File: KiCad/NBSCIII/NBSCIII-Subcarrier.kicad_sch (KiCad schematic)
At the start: 7 parts, among them U4 4011, U5 4029, U6 4029, U7 4027, U8 4027

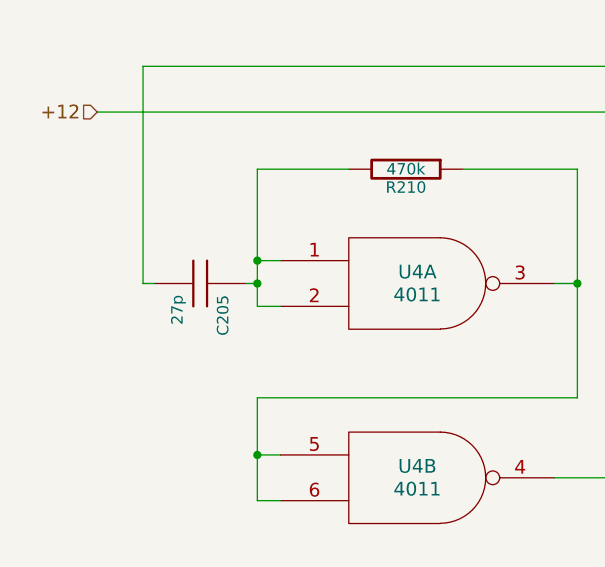
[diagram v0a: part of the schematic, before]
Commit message: unrescue to Device:C
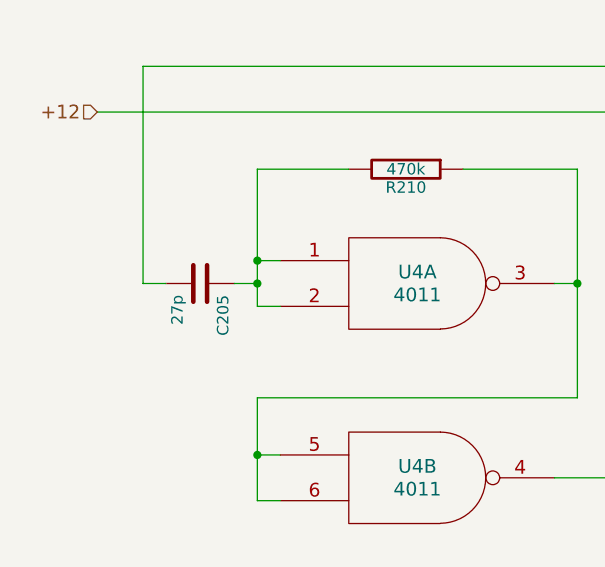
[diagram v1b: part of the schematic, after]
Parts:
- C205: symbol NBSCIII-rescue:C -> Device:C
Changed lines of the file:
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@@
-    (stroke (width 0) (type default) (color 0 0 0 0))
-  )
-  (wire (pts (xy 40.64 97.79) (xy 41.91 97.79))
     (stroke (width 0) (type default) (color 0 0 0 0))
   )
@@
     (stroke (width 0) (type default) (color 0 0 0 0))
   )
-  (wire (pts (xy 30.48 97.79) (xy 29.21 97.79))
+  (wire (pts (xy 29.21 97.79) (xy 31.75 97.79))
     (stroke (width 0) (type default) (color 0 0 0 0))
   )
@@
   )
   (wire (pts (xy 87.63 176.53) (xy 87.63 191.77))
+    (stroke (width 0) (type default) (color 0 0 0 0))
+  )
+  (wire (pts (xy 39.37 97.79) (xy 41.91 97.79))
     (stroke (width 0) (type default) (color 0 0 0 0))
   )
@@
     (pin "2")
   )
-  (symbol (lib_id "NBSCIII-rescue:C") (at 35.56 97.79 270) (unit 1)
+  (symbol (lib_id "Device:C") (at 35.56 97.79 270) (unit 1)
     (in_bom yes) (on_board yes)
     (property "Reference" "C205" (id 0) (at 38.1 99.06 0)

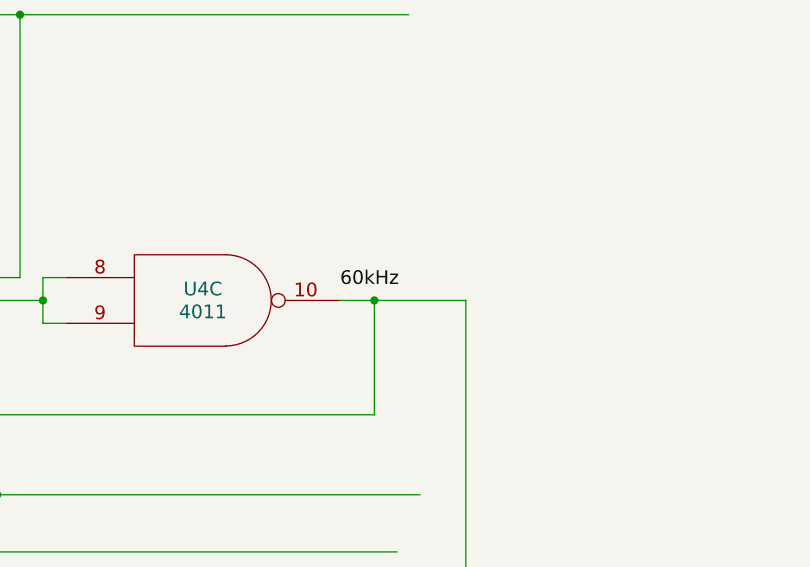
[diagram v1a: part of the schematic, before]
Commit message: unrescue to Device:C_Polarized
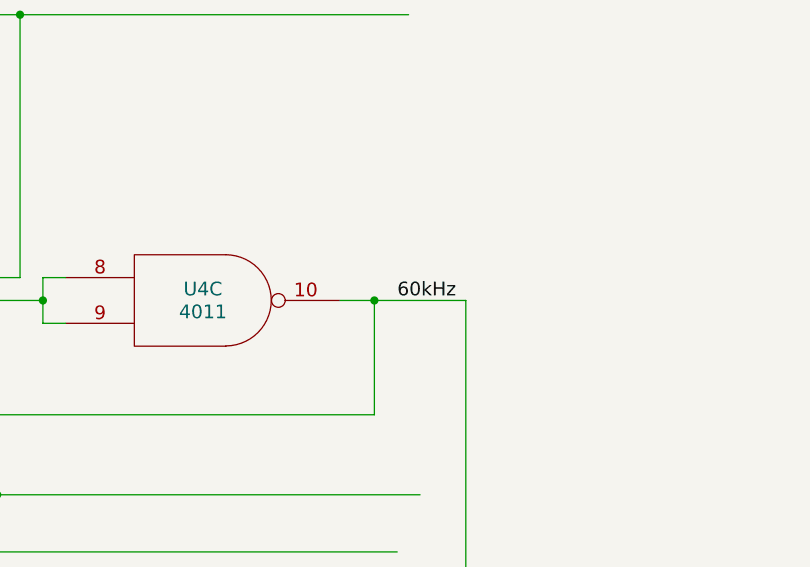
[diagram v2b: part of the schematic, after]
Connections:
- net 60kHz: now also U4.10, U5.1 (PE), U6.1 (PE), U7.3 (Cp), U8.3 (Cp)
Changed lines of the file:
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@@
     (effects (font (size 1.524 1.524)) (justify left bottom))
   )
-  (label "60kHz" (at 210.82 109.22 0)
+  (label "60kHz" (at 217.17 110.49 0)
     (effects (font (size 1.524 1.524)) (justify left bottom))
   )

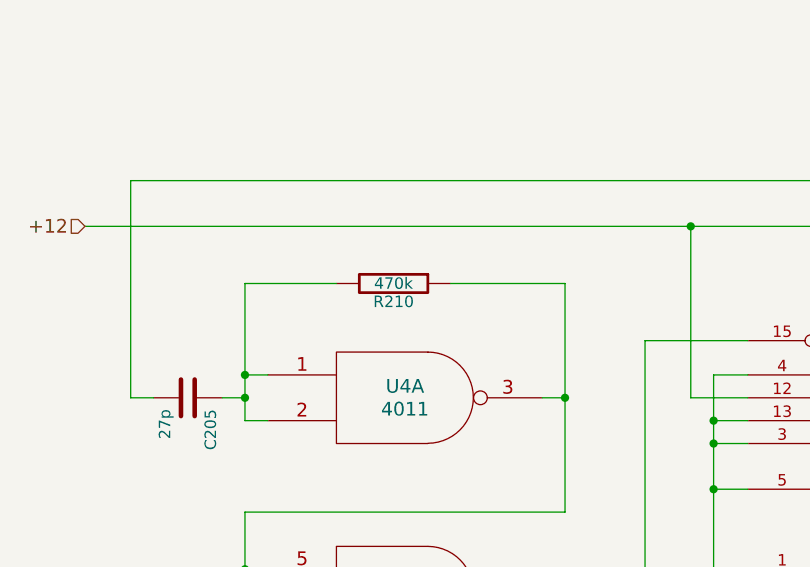
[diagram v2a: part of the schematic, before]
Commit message: unrescue Device:R
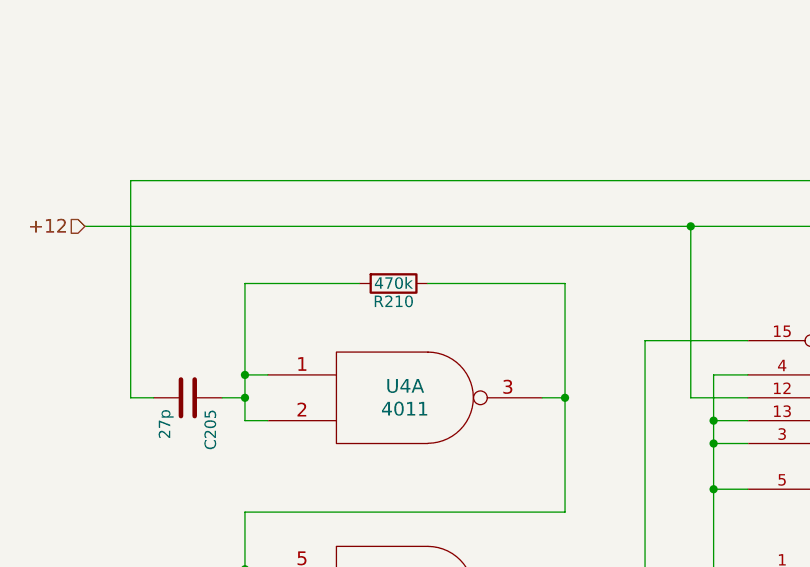
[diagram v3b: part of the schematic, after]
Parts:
- R210: symbol NBSCIII-rescue:R -> Device:R
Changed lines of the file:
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@@
     (stroke (width 0) (type default) (color 0 0 0 0))
   )
-  (wire (pts (xy 77.47 85.09) (xy 64.77 85.09))
+  (wire (pts (xy 77.47 85.09) (xy 62.23 85.09))
     (stroke (width 0) (type default) (color 0 0 0 0))
   )
@@
     (stroke (width 0) (type default) (color 0 0 0 0))
   )
-  (wire (pts (xy 41.91 85.09) (xy 52.07 85.09))
+  (wire (pts (xy 41.91 85.09) (xy 54.61 85.09))
     (stroke (width 0) (type default) (color 0 0 0 0))
   )
@@
     (pin "13")
   )
-  (symbol (lib_id "NBSCIII-rescue:R") (at 58.42 85.09 270) (unit 1)
+  (symbol (lib_id "Device:R") (at 58.42 85.09 270) (unit 1)
     (in_bom yes) (on_board yes)
     (property "Reference" "R210" (id 0) (at 58.42 87.122 90))

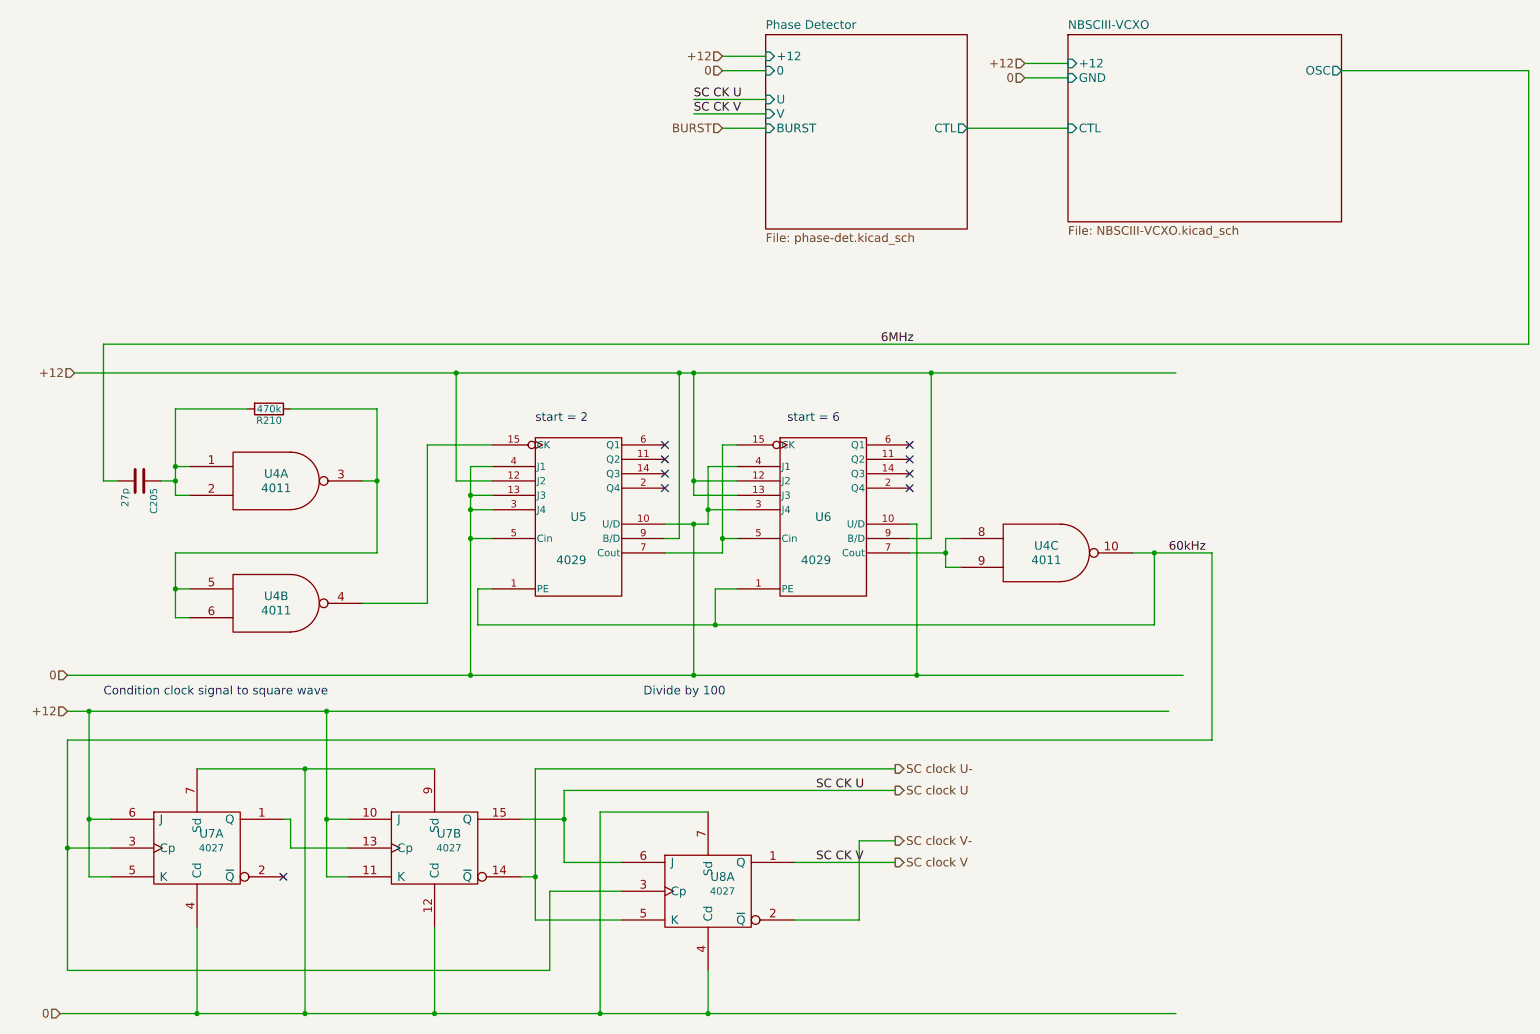
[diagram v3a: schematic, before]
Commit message: Simplify power distribution and make global
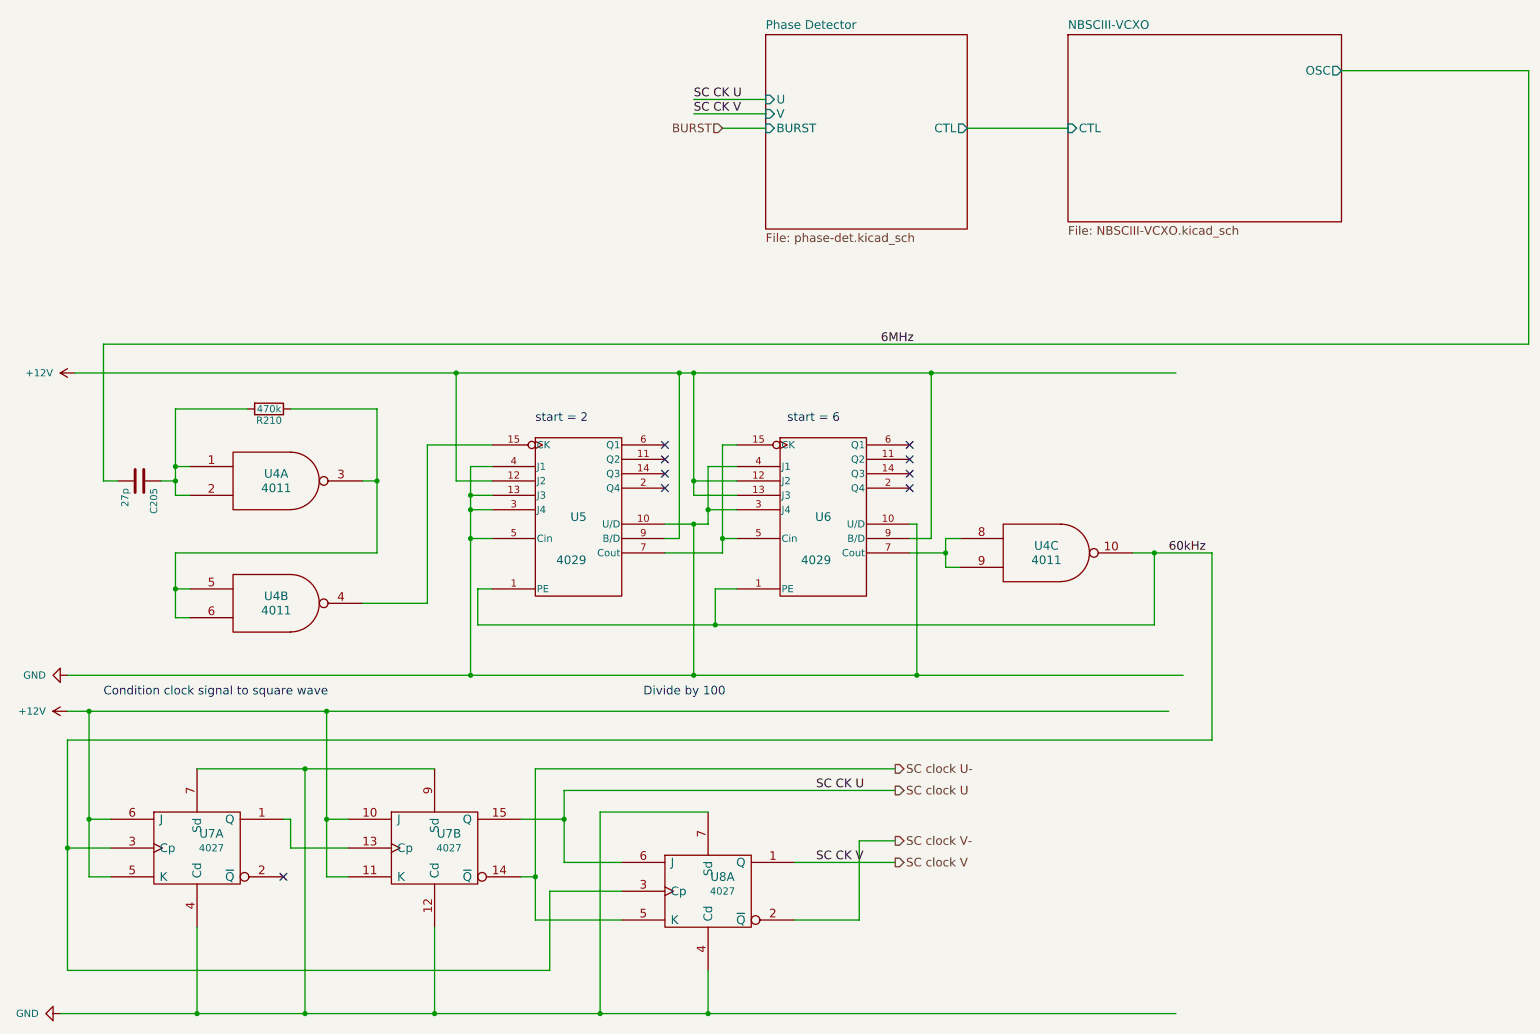
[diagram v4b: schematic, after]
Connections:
- net +12 renamed +12V
- net 0 renamed GND
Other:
- sheet NBSCIII-VCXO ports: added none; removed +12, GND
- sheet Phase Detector ports: added none; removed +12, 0
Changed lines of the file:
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@@
-    (stroke (width 0) (type default) (color 0 0 0 0))
-  )
-  (wire (pts (xy 146.05 22.86) (xy 138.43 22.86))
     (stroke (width 0) (type default) (color 0 0 0 0))
   )
@@
     (stroke (width 0) (type default) (color 0 0 0 0))
   )
-  (wire (pts (xy 199.39 26.67) (xy 191.77 26.67))
-    (stroke (width 0) (type default) (color 0 0 0 0))
-  )
   (wire (pts (xy 41.91 95.25) (xy 44.45 95.25))
     (stroke (width 0) (type default) (color 0 0 0 0))
@@
     (stroke (width 0) (type default) (color 0 0 0 0))
   )
-  (wire (pts (xy 146.05 25.4) (xy 138.43 25.4))
-    (stroke (width 0) (type default) (color 0 0 0 0))
-  )
   (wire (pts (xy 41.91 116.84) (xy 41.91 110.49))
     (stroke (width 0) (type default) (color 0 0 0 0))
@@
     (stroke (width 0) (type default) (color 0 0 0 0))
   )
-  (wire (pts (xy 199.39 24.13) (xy 191.77 24.13))
-    (stroke (width 0) (type default) (color 0 0 0 0))
-  )
   (wire (pts (xy 177.8 113.03) (xy 177.8 110.49))
     (stroke (width 0) (type default) (color 0 0 0 0))
@@
   (label "6MHz" (at 166.37 73.66 0)
     (effects (font (size 1.524 1.524)) (justify left bottom))
-  )
-  (hierarchical_label "+12" (shape input) (at 138.43 22.86 180)
-    (effects (font (size 1.524 1.524)) (justify right))
   )
   (hierarchical_label "BURST" (shape input) (at 138.43 35.56 180)
@@
     (effects (font (size 1.524 1.524)) (justify left))
   )
-  (hierarchical_label "+12" (shape input) (at 191.77 24.13 180)
-    (effects (font (size 1.524 1.524)) (justify right))
-  )
-  (hierarchical_label "0" (shape input) (at 22.86 132.08 180)
-    (effects (font (size 1.524 1.524)) (justify right))
-  )
-  (hierarchical_label "0" (shape input) (at 191.77 26.67 180)
-    (effects (font (size 1.524 1.524)) (justify right))
-  )
-  (hierarchical_label "+12" (shape input) (at 24.13 78.74 180)
-    (effects (font (size 1.524 1.524)) (justify right))
-  )
-  (hierarchical_label "+12" (shape input) (at 22.86 138.43 180)
-    (effects (font (size 1.524 1.524)) (justify right))
-  )
-  (hierarchical_label "0" (shape input) (at 21.59 191.77 180)
-    (effects (font (size 1.524 1.524)) (justify right))
-  )
   (hierarchical_label "SC clock U" (shape output) (at 168.91 152.4 0)
     (effects (font (size 1.524 1.524)) (justify left))
@@
   (hierarchical_label "SC clock U-" (shape output) (at 168.91 148.59 0)
     (effects (font (size 1.524 1.524)) (justify left))
-  )
-  (hierarchical_label "0" (shape input) (at 138.43 25.4 180)
-    (effects (font (size 1.524 1.524)) (justify right))
   )
   (symbol (lib_id "NBSCIII-rescue:4011") (at 59.69 97.79 0) (unit 1)
@@
     (pin "15")
     (pin "9")
+  )
+  (symbol (lib_id "power:+12V") (at 24.13 78.74 90) (unit 1)
+    (in_bom yes) (on_board yes) (fields_autoplaced)
+    (property "Reference" "#PWR0122" (id 0) (at 27.94 78.74 0)
+      (effects (font (size 1.27 1.27)) hide)
+    )
+    (property "Value" "+12V" (id 1) (at 20.32 78.7399 90)
+      (effects (font (size 1.27 1.27)) (justify left))
+    )
+    (property "Footprint" "" (id 2) (at 24.13 78.74 0)
+      (effects (font (size 1.27 1.27)) hide)
+    )
+    (property "Datasheet" "" (id 3) (at 24.13 78.74 0)
+      (effects (font (size 1.27 1.27)) hide)
+    )
+    (pin "1")
+  )
+  (symbol (lib_id "power:GND") (at 21.59 191.77 270) (unit 1)
+    (in_bom yes) (on_board yes) (fields_autoplaced)
+    (property "Reference" "#PWR0125" (id 0) (at 15.24 191.77 0)
+      (effects (font (size 1.27 1.27)) hide)
+    )
+    (property "Value" "GND" (id 1) (at 17.78 191.7699 90)
+      (effects (font (size 1.27 1.27)) (justify right))
+    )
+    (property "Footprint" "" (id 2) (at 21.59 191.77 0)
+      (effects (font (size 1.27 1.27)) hide)
+    )
+    (property "Datasheet" "" (id 3) (at 21.59 191.77 0)
+      (effects (font (size 1.27 1.27)) hide)
+    )
+    (pin "1")
+  )
+  (symbol (lib_id "power:+12V") (at 22.86 138.43 90) (unit 1)
+    (in_bom yes) (on_board yes) (fields_autoplaced)
+    (property "Reference" "#PWR0123" (id 0) (at 26.67 138.43 0)
+      (effects (font (size 1.27 1.27)) hide)
+    )
+    (property "Value" "+12V" (id 1) (at 19.05 138.4299 90)
+      (effects (font (size 1.27 1.27)) (justify left))
+    )
+    (property "Footprint" "" (id 2) (at 22.86 138.43 0)
+      (effects (font (size 1.27 1.27)) hide)
+    )
+    (property "Datasheet" "" (id 3) (at 22.86 138.43 0)
+      (effects (font (size 1.27 1.27)) hide)
+    )
+    (pin "1")
+  )
+  (symbol (lib_id "power:GND") (at 22.86 132.08 270) (unit 1)
+    (in_bom yes) (on_board yes) (fields_autoplaced)
+    (property "Reference" "#PWR0124" (id 0) (at 16.51 132.08 0)
+      (effects (font (size 1.27 1.27)) hide)
+    )
+    (property "Value" "GND" (id 1) (at 19.05 132.0799 90)
+      (effects (font (size 1.27 1.27)) (justify right))
+    )
+    (property "Footprint" "" (id 2) (at 22.86 132.08 0)
+      (effects (font (size 1.27 1.27)) hide)
+    )
+    (property "Datasheet" "" (id 3) (at 22.86 132.08 0)
+      (effects (font (size 1.27 1.27)) hide)
+    )
+    (pin "1")
   )
   (sheet (at 199.39 19.05) (size 48.26 33.02) (fields_autoplaced)
@@
       (effects (font (size 1.524 1.524)) (justify left))
     )
-    (pin "+12" input (at 199.39 24.13 180)
-      (effects (font (size 1.524 1.524)) (justify left))
-    )
-    (pin "GND" input (at 199.39 26.67 180)
-      (effects (font (size 1.524 1.524)) (justify left))
-    )
     (pin "OSC" output (at 247.65 25.4 0)
       (effects (font (size 1.524 1.524)) (justify right))
@@
       (effects (font (size 1.524 1.524)) (justify left))
     )
-    (pin "0" input (at 146.05 25.4 180)
-      (effects (font (size 1.524 1.524)) (justify left))
-    )
-    (pin "+12" input (at 146.05 22.86 180)
-      (effects (font (size 1.524 1.524)) (justify left))
-    )

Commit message: unrescue 4011, R
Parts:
- added unit 4 of U4
- added unit 5 of U4
- R210: value 470k -> 220k
- U4: symbol NBSCIII-rescue:4011 -> 4xxx:4011
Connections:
- net +12V: now also U4.14 (VDD)
- net GND: now also U4.12, U4.13, U4.7 (VSS)
- net VDD: no longer U4.14 (VDD), U4.14 (VDD), U4.14 (VDD)
- net VSS: no longer U4.7 (VSS), U4.7 (VSS), U4.7 (VSS)
- no-connect marks 9 -> 10

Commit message: unrescue 4029
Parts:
- U5, U6: symbol NBSCIII-rescue:4029 -> 4xxx:4029
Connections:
- net +12V: now also U5.16 (VDD), U6.16 (VDD)
- net GND: now also U5.8 (VSS), U6.8 (VSS)
- net VDD: no longer U5.16 (VDD), U6.16 (VDD)
- net VSS: no longer U5.8 (VSS), U6.8 (VSS)

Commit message: derescue 4027
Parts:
- added C206, C207, C208: 100n, symbol Device:C
- added unit 3 of U7
- added unit 3 of U8
- added unit 2 of U8
- U7, U8: symbol NBSCIII-rescue:4027 -> 4xxx:4027
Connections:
- net +12V: now also C206.1, C207.1, C208.1, U7.16 (VDD), U8.16 (VDD)
- net GND: now also C206.2, C207.2, C208.2, U7.8 (VSS), U8.10 (J), U8.11 (K), U8.12 (R), U8.13 (C), U8.8 (VSS), U8.9 (S)
- removed net VDD: U7.16 (VDD), U7.16 (VDD), U8.16 (VDD)
- removed net VSS: U7.8 (VSS), U7.8 (VSS), U8.8 (VSS)
- no-connect marks 10 -> 12
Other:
- moved on the sheet: U4D, U8A
